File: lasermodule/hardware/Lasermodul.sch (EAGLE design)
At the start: 66 parts, among them IC1 MEGA8-AI

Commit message: the real real Hitpoint 1.0
so wurden die ersten 20 platinen bestellt
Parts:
- added K3G1, K3G2, K3G3, K3G4, K3G5, K3G6: (no value), wz:PIN-HEADER-1
- +5V, B+, B-, GND, I+, I-, K1, K1G, K2, K2G, K3, K3G, L+1, L+2, L+3, LB, LG, LR, T5V, TB, TG, TR, TW: device wz:PINHD-1X1 -> wz:PIN-HEADER-1
- BUS, ZUM_PI: value 04-JST-B4B-XH-A -> JST-XH_BUCHSE-4-; device wz:04-JST-B4B-XH-A -> wz:JST-XH_BUCHSE-4-
- C1, C4, C5: device wz:C-EUC0805 -> wz:C_EU0603
- C10, C7, C8, C9: device wz:C-EUC0805 -> wz:C_EU0805
- C2: value 100u -> 4.7u; device wz_c:C-EUC1808 -> wz:C_EU0805
- C3: value 100u -> 1000u; device wz_c:C-EUC1808 -> wz:C_EUCAP_UNIVERSAL
- C6: device rcl:C-EUC0805 -> wz:C_EU0603
- D1: device wz:BZY97 -> wz:Z-DIODE
- D2: device wz:TVSARRAY_5LANE -> wz:ESD-SCHUTZ
- LM1117: value V_REG_MIC2920 -> LM1117_3V3_REGULATOR; device wz:V_REG_MIC2920 -> wz:LM1117_3V3_REGULATOR
- R1, R10, R11, R12, R13, R14, R15, R2, R3, R6, R7, R8, R9: device rcl:R-EU_R0805 -> wz:R_EU0603
- R16, R4, R5: device wz:R-EU_R0805 -> wz:R_EU0603
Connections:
- new net N$34: K3G3.1, U$3.IN+
- net +5V: now also K3G1.1, K3G6.1, U$3.OUT+, U$4.VCC
- net GND: now also K3G2.1, K3G4.1, K3G5.1, U$3.GND, U$4.AGND, U$4.PGND
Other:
- moved on the sheet: DISPLAY, PI

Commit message: laserbodul hardware weiter gemacht
umstellung auf pi modul mit fast allem drauf
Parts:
- removed K3G1, K3G2, K3G3, K3G4, K3G5, K3G6: (no value), wz:PIN-HEADER-1
- added AMP_5V, AMP_GND, AMP_IN_L, AMP_IN_R, AMP_OUT_L_+, AMP_OUT_L_-, AMP_OUT_R_+, AMP_OUT_R_-, LIPO+, LIPO-, MISC_5V, MISC_GND: (no value), wz:PIN-HEADER-1
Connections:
- new net N$35: AMP_IN_L.1, U$4.IN_L
- new net N$36: AMP_IN_R.1, U$4.IN_R
- new net N$37: AMP_OUT_L_+.1, U$4.OUT_L_+
- new net N$38: AMP_OUT_L_-.1, U$4.OUT_L_-
- new net N$39: AMP_OUT_R_-.1, U$4.OUT_R_-
- new net N$40: AMP_OUT_R_+.1, U$4.OUT_R_+
- net +5V: now also AMP_5V.1, MISC_5V.1; no longer K3G1.1, K3G6.1
- net GND: now also AMP_GND.1, LIPO-.1, MISC_GND.1; no longer K3G2.1, K3G4.1, K3G5.1
- net N$34: now also LIPO+.1; no longer K3G3.1
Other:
- note added: "Audio amplifier"
- note added: "IR Reciever"
- note added: "LiPo-Connector --> 5V Step-Up --> 3.3V Regulator"
- moved on the sheet: C1, C2, C3, C6, LM1117

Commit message: weiter gemacht
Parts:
- removed +5V, AMP_5V, AMP_GND, GND, L+3, LB, LG, LIPO+, LIPO-, LR, MISC_5V, MISC_GND: (no value), wz:PIN-HEADER-1
- removed ZUM_PI: JST-XH_BUCHSE-4-, wz:JST-XH_BUCHSE-4-
- added EXT_+5V, EXT_GND, EXT_SCL_BUS, EXT_SDA_BUS, KEY_OFF_1, KEY_OFF_2, KEY_ON_1, KEY_ON_2, L1, L2: (no value), wz:PIN-HEADER-1
- added Q1: (no value), wz:CEG8205_DOPPEL_N_FET
- added R17: 47k, wz:R_EU0603
- DISPLAY: device con-lstb:MA12-1 -> wz:PIN-HEADER-DISPLAY
- R1: value 100 -> (none)
- R3: value (none) -> 100k
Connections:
- net LASER_G renamed LASER_2
- net N$1 renamed I_LED_R
- net N$10 renamed I_LED_B
- net N$17 renamed TX
- net N$2 renamed I_LED_G
- net N$26 renamed AMBI_LIGHT
- net N$3 renamed I_IR_TAKT_-
- net N$7 renamed I_LASER_2
- net N$8 renamed I_LED_W
- net N$9 renamed I_LASER_1
- removed net LASER_B: R3.1, ULN2803.O6
- removed net LASER_R: R1.1, ULN2803.O4
- removed net N$14: C5.2, IC1.PC2(ADC2), R4.1, R5.2
- removed net N$19: LB.1, R3.2
- removed net N$27: R7.1, ZUM_PI-4.1
- removed net N$28: R6.1, ZUM_PI-3.1
- removed net N$34: LIPO+.1, U$3.IN+
- removed net N$4: IC1.PB0(ICP), ULN2803.I4
- removed net SCL: BUS-4.1, D2.C3, IC1.PC5(ADC5/SCL), R7.2
- removed net SDA: BUS-3.1, D2.C2, IC1.PC4(ADC4/SDA), R6.2
- removed net V_BATT: B+.1, R4.2
- new net BACKLIGHT: DISPLAY.8, ULN2803.O4
- new net BATT_+: B+.1, KEY_ON_2.1, R4.2, U$3.IN+
- new net BATT_-: B-.1, Q1.S1, R3.2
- new net I_BACKLIGHT: PI.12, ULN2803.I4
- new net LASER_1: R1.1, ULN2803.O6
- new net N$1: DISPLAY.14, PI.13
- new net N$2: DISPLAY.11, PI.26
- new net N$26: KEY_ON_1.1, R17.1
- new net N$44: DISPLAY.1, PI.1
- new net N$45: DISPLAY.2, PI.9
- new net N$47: DISPLAY.5, PI.18
- new net N$48: DISPLAY.12, DISPLAY.6, PI.19
- new net N$49: DISPLAY.13, DISPLAY.9, PI.21
- new net N$50: DISPLAY.4, PI.22
- new net N$51: DISPLAY.10, DISPLAY.7, PI.23
- new net N$52: DISPLAY.3, PI.24
- new net ONOFF: IC1.PD2(INT0), KEY_OFF_1.1, Q1.G1, R17.2, R3.1
- new net SCL_BUS: BUS-4.1, D2.C3, EXT_SCL_BUS.1, IC1.PC5(ADC5/SCL), R7.2
- new net SCL_PI: PI.5, R7.1
- new net SDA_BUS: BUS-3.1, D2.C2, EXT_SDA_BUS.1, IC1.PC4(ADC4/SDA), R6.2
- new net SDA_PI: PI.3, R6.1
- new net V_BATT_LOW: C5.1, IC1.PC2(ADC2), R4.1, R5.2
- net +5V: now also EXT_+5V.1, PI.2, PI.4; no longer +5V.1, AMP_5V.1, MISC_5V.1, ZUM_PI-2.1
- net GND: now also C5.2, EXT_GND.1, KEY_OFF_2.1, PI.6, Q1.D; no longer AMP_GND.1, B-.1, C5.1, GND.1, LIPO-.1, MISC_GND.1, ZUM_PI-1.1
- net LASER_+: no longer L+3.1
- net N$12: now also L1.1; no longer LR.1
- net N$18: now also L2.1; no longer LG.1
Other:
- note added: "Ambient light sensor"
- note added: "Battery --> 5V Step-Up --> 3.3V Regulator"
- note added: "Battery connector"
- note added: "Battery voltage sensor"
- note added: "Buttons"
- note added: "ESD and i2c bus protection"
- note added: "Extension port"
- note added: "IR LED connector"
- note added: "IR LED driver"
- note added: "Laser connector with over voltage protection"
- note added: "Pi- and Display-connector"
- note added: "Poweroff"
- note added: "Signal amplifier"
- note removed: "Laser connector"
- note removed: "LiPo-Connector --> 5V Step-Up --> 3.3V Regulator"
- note removed: "Raspberry Pi connector"
- moved on the sheet: AMP_IN_L, AMP_IN_R, AMP_OUT_L_+, AMP_OUT_L_-, AMP_OUT_R_+, AMP_OUT_R_-, B+, B-, BUS-1, BUS-2, BUS-3, BUS-4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

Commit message: ...
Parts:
- removed Q1: (no value), wz:CEG8205_DOPPEL_N_FET
- added R18: 10k, wz:R_EU0603
- added STEP_UP_ENABLE: (no value), wz:PIN-HEADER-1
- R17: value 47k -> 1k
- R3: value 100k -> 10k
- R5: value 10k -> 180k
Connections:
- removed net BATT_-: B-.1, Q1.S1, R3.2
- net GND: now also B-.1, R3.2; no longer Q1.D
- net ONOFF: now also R18.1, R18.2, STEP_UP_ENABLE.1; no longer Q1.G1
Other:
- note added: "Ambient light sensor (ref = vcc)"
- note added: "Battery voltage sensor (ref = vcc)"
- note removed: "Ambient light sensor"
- note removed: "Battery voltage sensor"
- moved on the sheet: D2, KEY_OFF_1, KEY_OFF_2, KEY_ON_1, KEY_ON_2, R17, R3, R6, R7

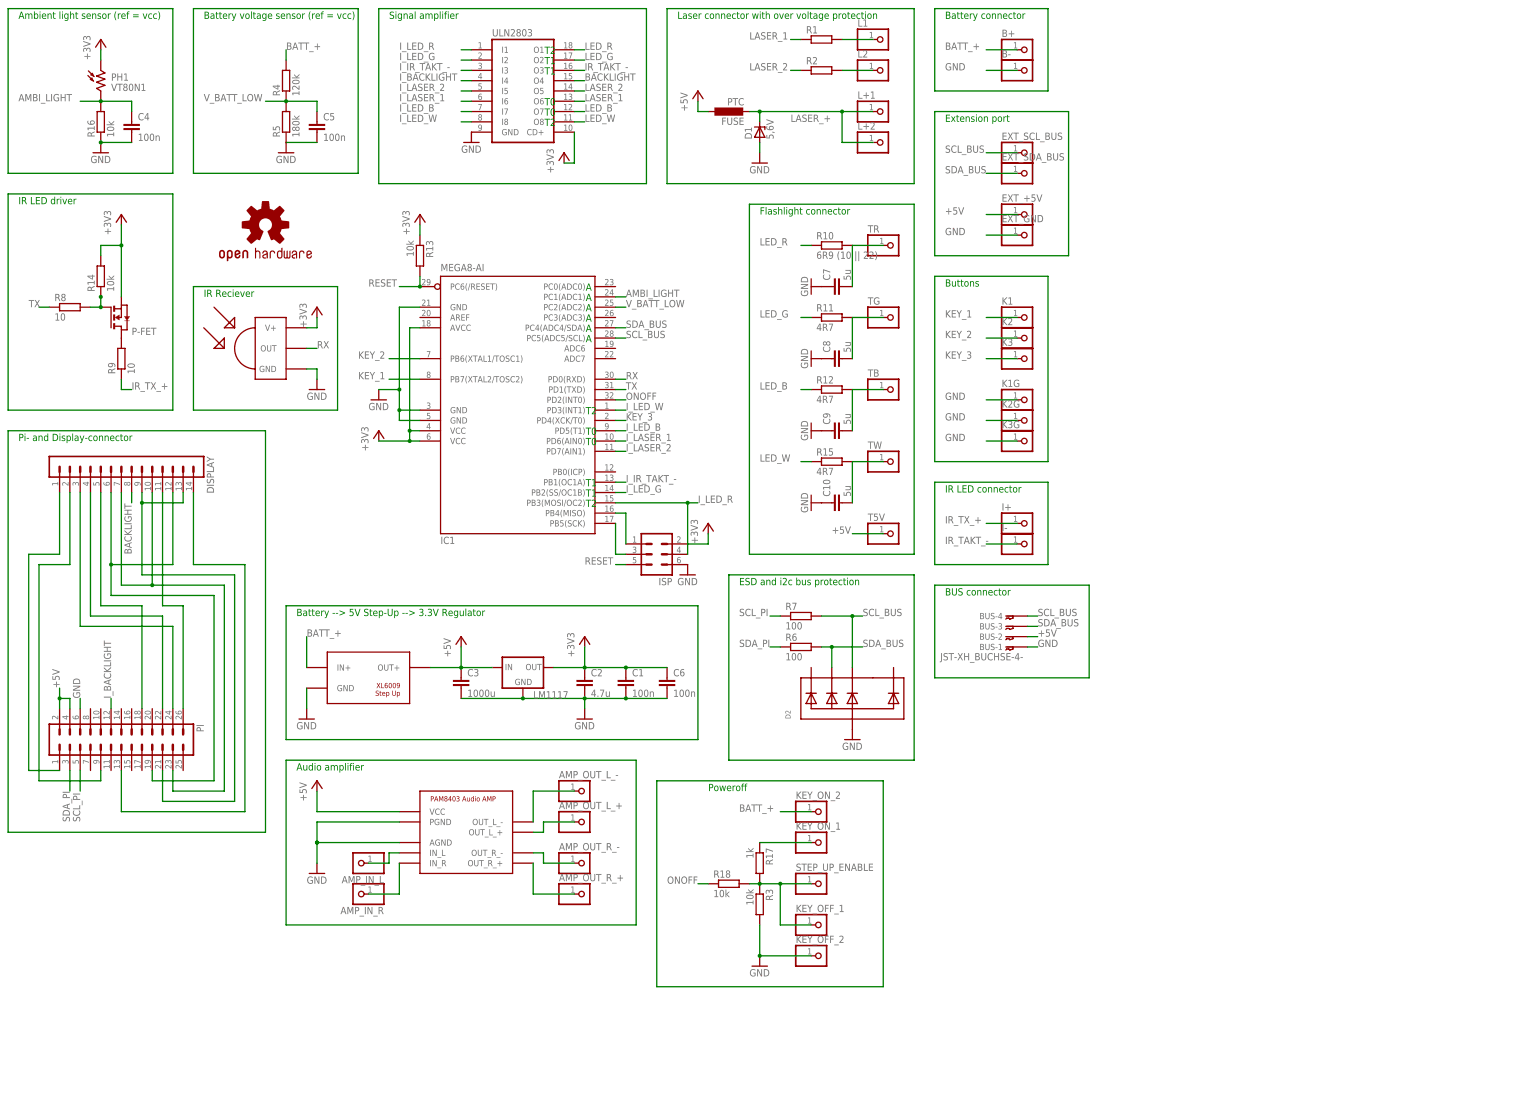
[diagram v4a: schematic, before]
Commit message: lasermodul schaltplan rc1
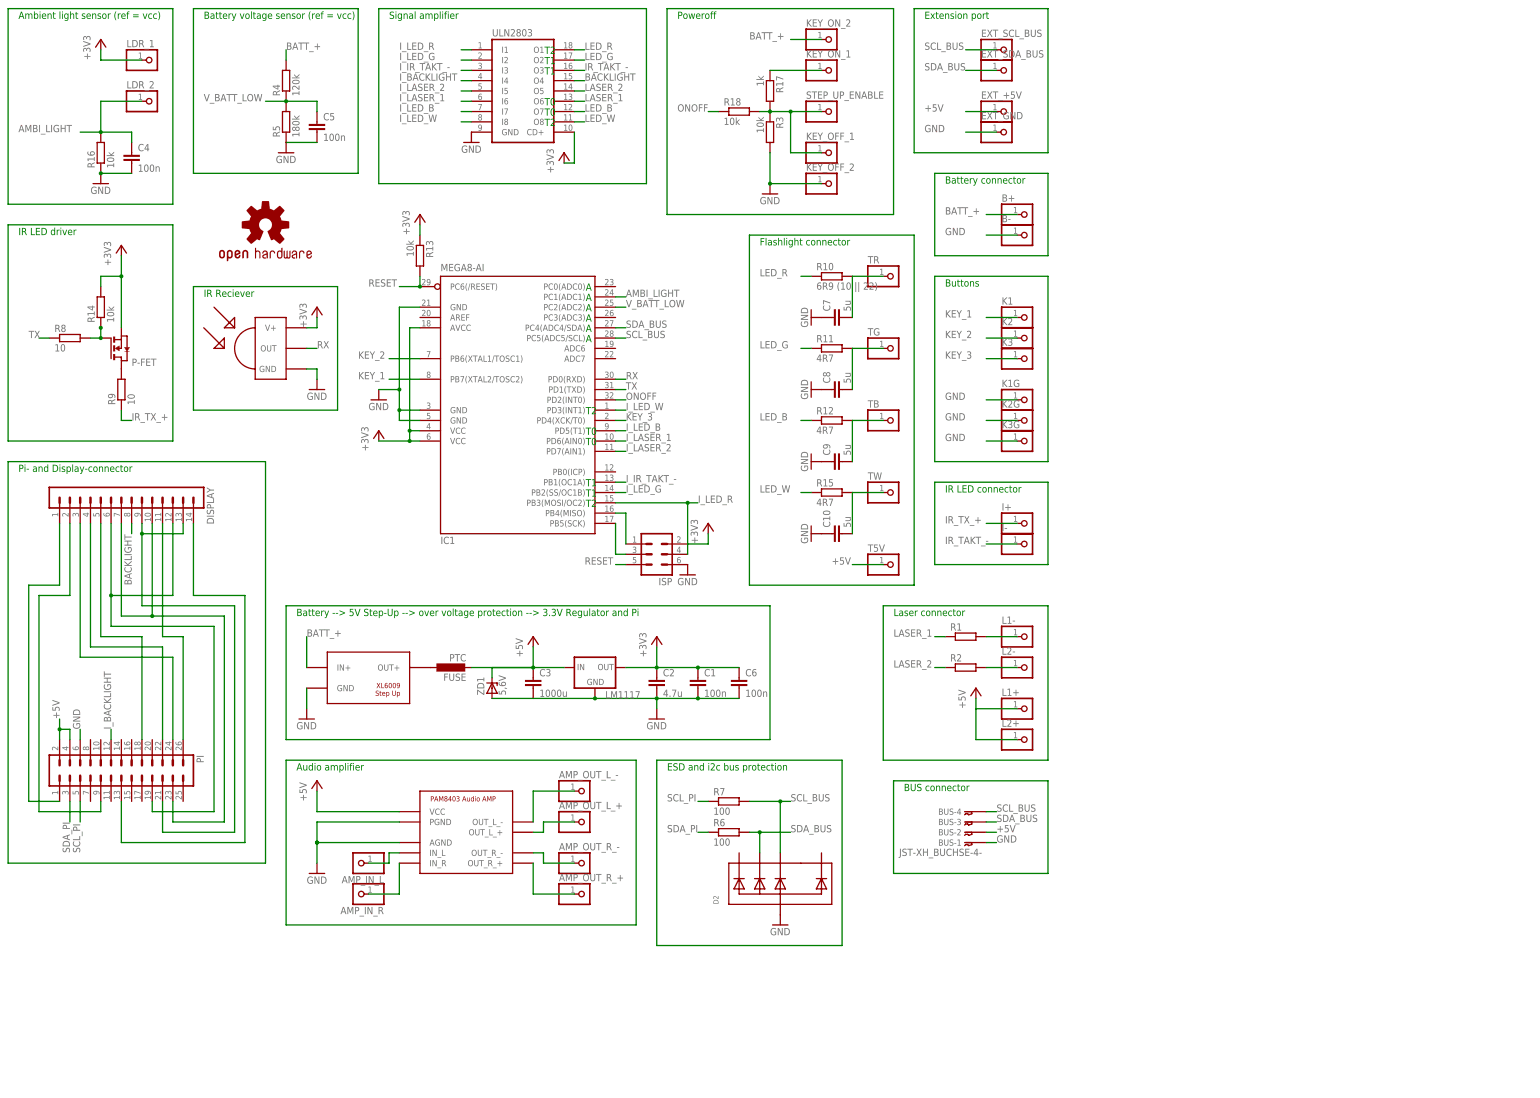
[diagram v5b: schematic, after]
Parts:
- removed D1: 5,6V, wz:Z-DIODE
- removed L+1, L+2, L1, L2: (no value), wz:PIN-HEADER-1
- removed PH1: VT80N1, photo-elements:VT80N1
- added L1+, L1-, L2+, L2-, LDR_1, LDR_2: (no value), wz:PIN-HEADER-1
- added ZD1: 5,6V, wz:Z-DIODE
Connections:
- removed net LASER_+: D1.C, FUSE.2, L+1.1, L+2.1
- new net N$28: FUSE.1, U$3.OUT+
- net +3V3: now also LDR_1.1; no longer PH1.1
- net +5V: now also FUSE.2, L1+.1, L2+.1, ZD1.C; no longer FUSE.1, U$3.OUT+
- net AMBI_LIGHT: now also LDR_2.1; no longer PH1.2
- net GND: now also ZD1.A; no longer D1.A
- net N$12: now also L1-.1; no longer L1.1
- net N$18: now also L2-.1; no longer L2.1
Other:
- note added: "Battery --> 5V Step-Up --> over voltage protection --> 3.3V Regulator and Pi"
- note added: "Laser connector"
- note removed: "Battery --> 5V Step-Up --> 3.3V Regulator"
- note removed: "Laser connector with over voltage protection"
- moved on the sheet: B+, B-, BUS-1, BUS-2, BUS-3, BUS-4, C1, C10, C2, C3, C4, C6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

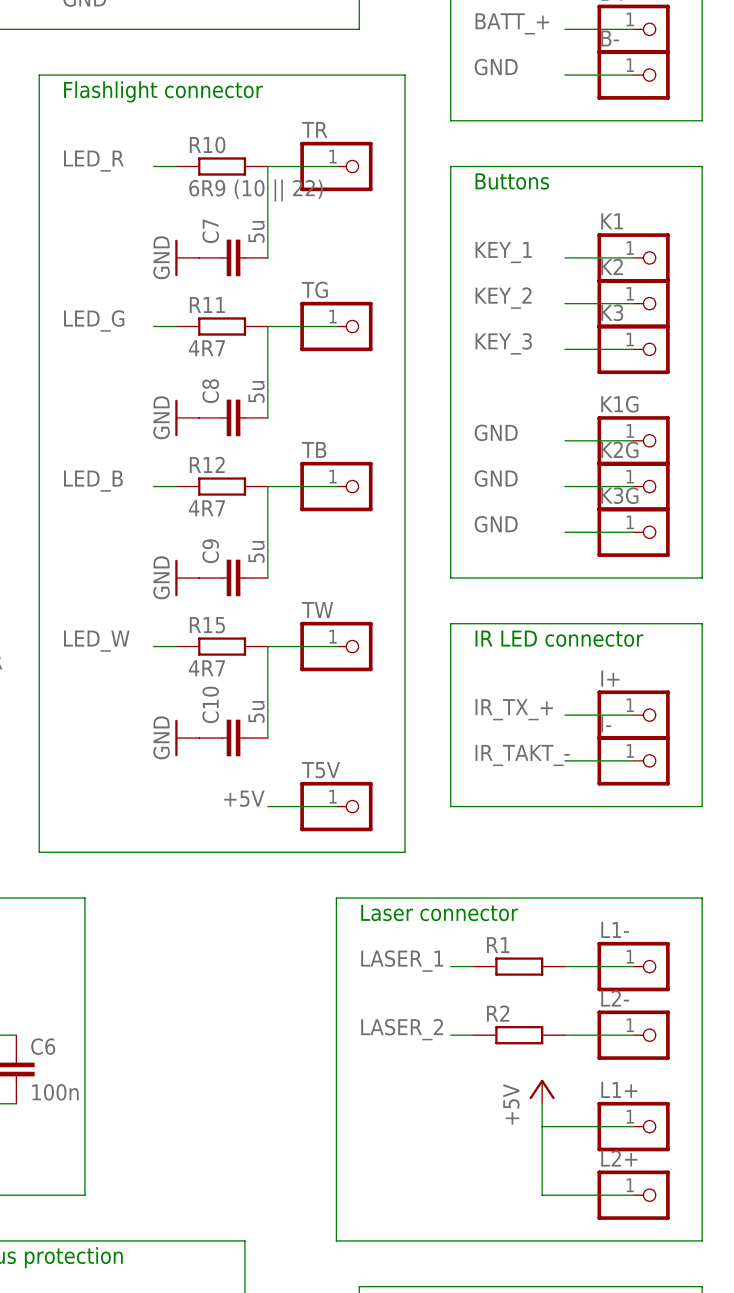
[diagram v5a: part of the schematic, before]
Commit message: started plexi tiefzieh case
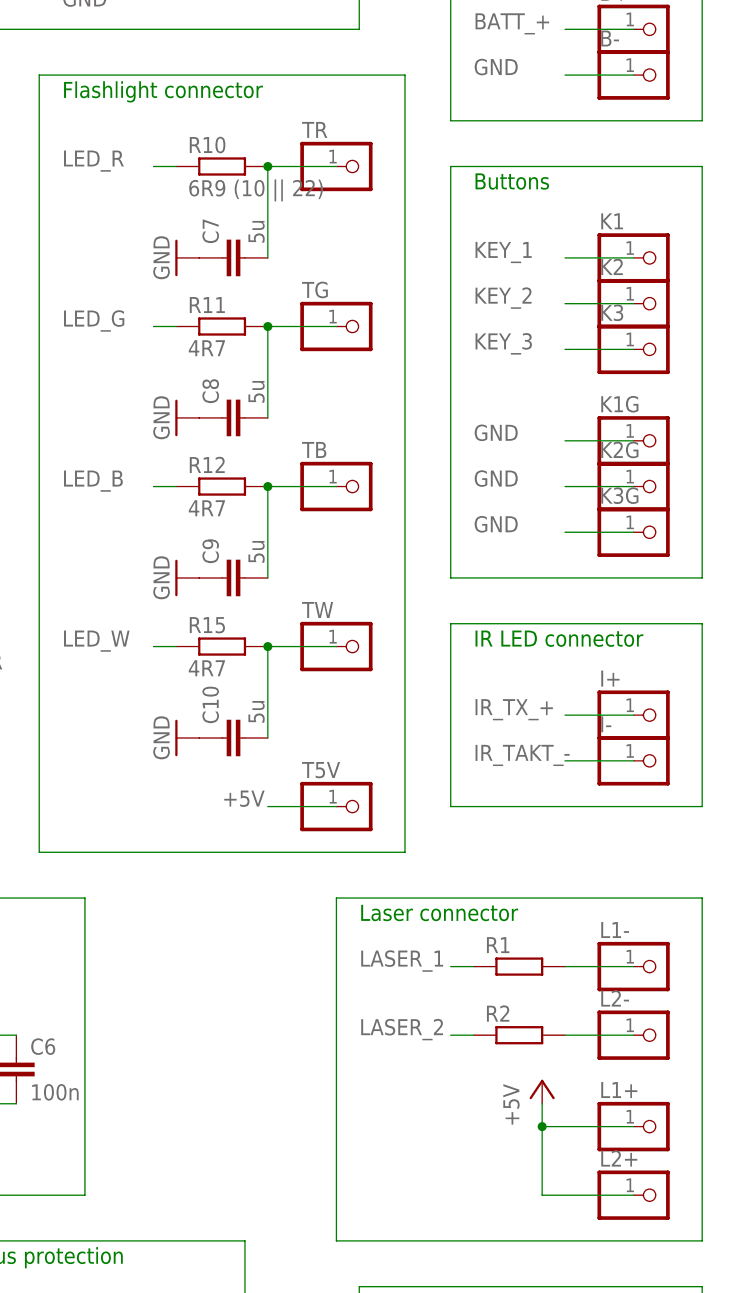
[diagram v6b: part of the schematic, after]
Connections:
- new net STEPUP_EN: KEY_OFF_1.1, R17.2, R18.2, R3.1, STEP_UP_ENABLE.1
- net ONOFF: no longer KEY_OFF_1.1, R17.2, R18.2, R3.1, STEP_UP_ENABLE.1
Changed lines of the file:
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@@
 <pinref part="P+2" gate="1" pin="+5V"/>
 <wire x1="147.32" y1="-40.64" x2="147.32" y2="-38.1" width="0.1524" layer="91"/>
+<junction x="147.32" y="-40.64"/>
 </segment>
 </net>
@@
 <pinref part="C7" gate="G$1" pin="2"/>
 <wire x1="116.84" y1="55.88" x2="116.84" y2="66.04" width="0.1524" layer="91"/>
+<junction x="116.84" y="66.04"/>
 </segment>
 </net>
@@
 <pinref part="C8" gate="G$1" pin="2"/>
 <wire x1="116.84" y1="48.26" x2="116.84" y2="38.1" width="0.1524" layer="91"/>
+<junction x="116.84" y="48.26"/>
 </segment>
 </net>
@@
 <pinref part="C9" gate="G$1" pin="2"/>
 <wire x1="116.84" y1="30.48" x2="116.84" y2="20.32" width="0.1524" layer="91"/>
+<junction x="116.84" y="30.48"/>
 </segment>
 </net>
@@
 <pinref part="C10" gate="G$1" pin="2"/>
 <wire x1="116.84" y1="12.7" x2="116.84" y2="2.54" width="0.1524" layer="91"/>
+<junction x="116.84" y="12.7"/>
 </segment>
 </net>
@@
 </segment>
 <segment>
+<pinref part="R18" gate="G$1" pin="1"/>
+<wire x1="83.82" y1="106.68" x2="81.28" y2="106.68" width="0.1524" layer="91"/>
+<label x="73.66" y="106.68" size="1.778" layer="95"/>
+</segment>
+</net>
+<net name="N$26" class="0">
+<segment>
+<pinref part="KEY_ON_1" gate="G$1" pin="1"/>
+<pinref part="R17" gate="G$1" pin="1"/>
+<wire x1="109.22" y1="116.84" x2="96.52" y2="116.84" width="0.1524" layer="91"/>
+</segment>
+</net>
+<net name="N$27" class="0">
+<segment>
+<wire x1="71.12" y1="81.28" x2="127" y2="81.28" width="0.1524" layer="91"/>
+<wire x1="127" y1="81.28" x2="127" y2="132.08" width="0.1524" layer="91"/>
+<wire x1="127" y1="132.08" x2="71.12" y2="132.08" width="0.1524" layer="91"/>
+<wire x1="71.12" y1="132.08" x2="71.12" y2="81.28" width="0.1524" layer="91"/>
+</segment>
+</net>
+<net name="N$28" class="0">
+<segment>
+<pinref part="U$3" gate="G$1" pin="OUT+"/>
+<pinref part="FUSE" gate="G$1" pin="1"/>
+</segment>
+</net>
+<net name="STEPUP_EN" class="0">
+<segment>
 <pinref part="R3" gate="G$1" pin="1"/>
 <wire x1="96.52" y1="106.68" x2="101.6" y2="106.68" width="0.1524" layer="91"/>
@@
 <pinref part="R18" gate="G$1" pin="2"/>
 </segment>
-<segment>
-<pinref part="R18" gate="G$1" pin="1"/>
-<wire x1="83.82" y1="106.68" x2="81.28" y2="106.68" width="0.1524" layer="91"/>
-<label x="73.66" y="106.68" size="1.778" layer="95"/>
-</segment>
-</net>
-<net name="N$26" class="0">
-<segment>
-<pinref part="KEY_ON_1" gate="G$1" pin="1"/>
-<pinref part="R17" gate="G$1" pin="1"/>
-<wire x1="109.22" y1="116.84" x2="96.52" y2="116.84" width="0.1524" layer="91"/>
-</segment>
-</net>
-<net name="N$27" class="0">
-<segment>
-<wire x1="71.12" y1="81.28" x2="127" y2="81.28" width="0.1524" layer="91"/>
-<wire x1="127" y1="81.28" x2="127" y2="132.08" width="0.1524" layer="91"/>
-<wire x1="127" y1="132.08" x2="71.12" y2="132.08" width="0.1524" layer="91"/>
-<wire x1="71.12" y1="132.08" x2="71.12" y2="81.28" width="0.1524" layer="91"/>
-</segment>
-</net>
-<net name="N$28" class="0">
-<segment>
-<pinref part="U$3" gate="G$1" pin="OUT+"/>
-<pinref part="FUSE" gate="G$1" pin="1"/>
-</segment>
 </net>
 </nets>
 </sheet>
 </sheets>
-<errors>
-</errors>
 </schematic>
 </drawing>
